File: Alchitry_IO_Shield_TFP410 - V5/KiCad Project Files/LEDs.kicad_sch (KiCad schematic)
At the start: 52 parts, among them Q1 Q_PMOS_SGD, Q2 Q_PMOS_SGD, Q3 Q_PMOS_SGD, Q4 Q_PMOS_SGD, SW1 SWL3, SW10 SW_DIP_x08, SW2 SWL1, SW3 SWL2, SW4 SWL4, SW5 SWR3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

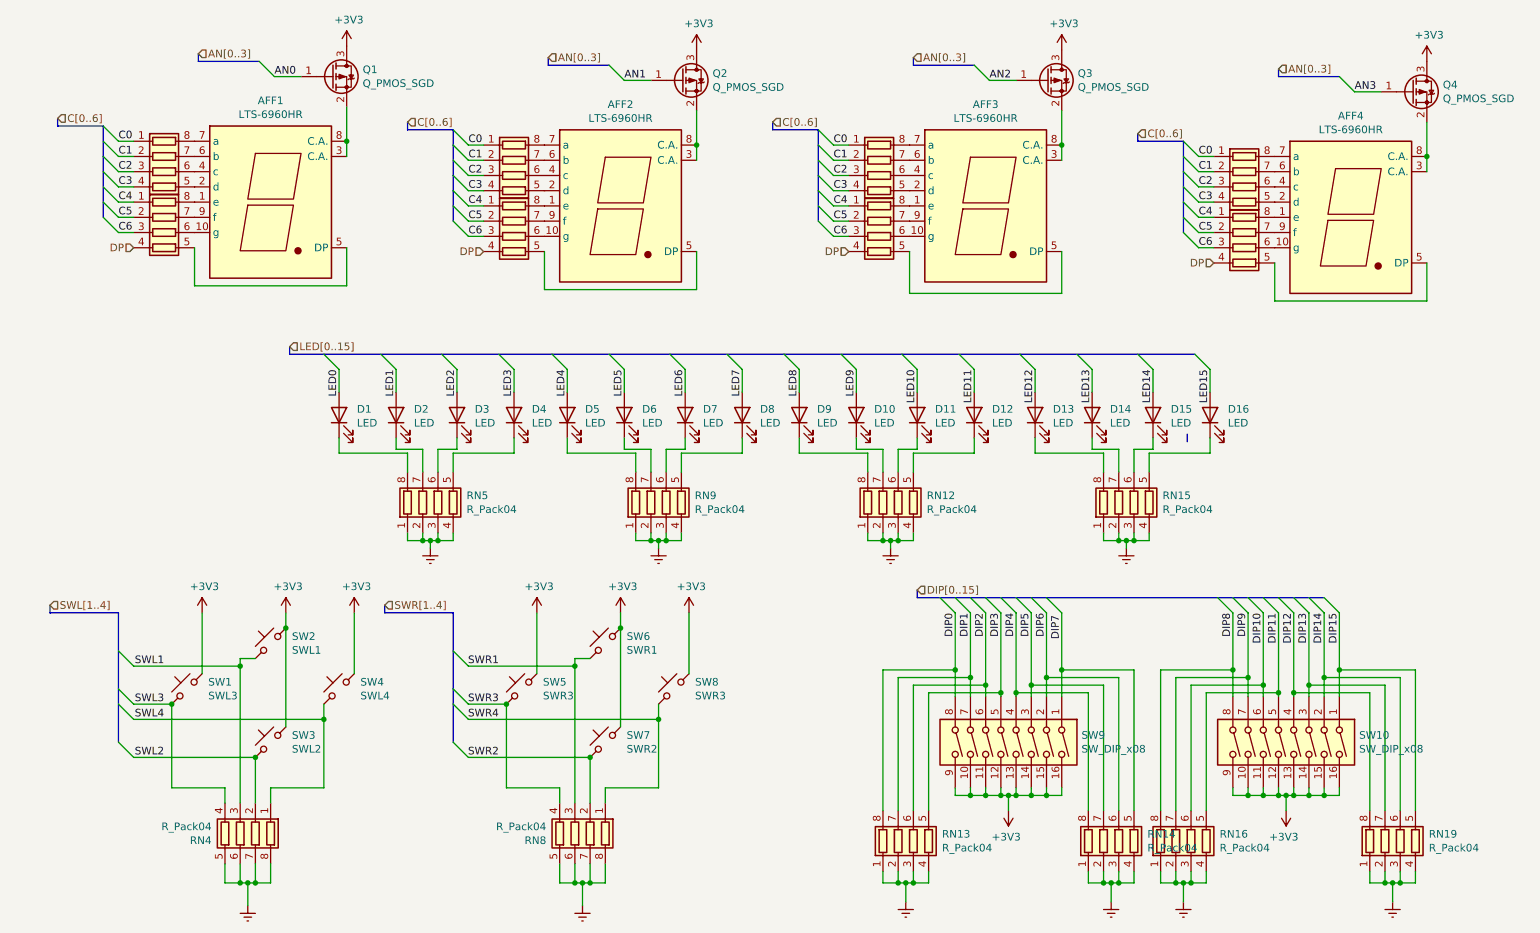
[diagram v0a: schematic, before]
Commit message: grouped footprints by function
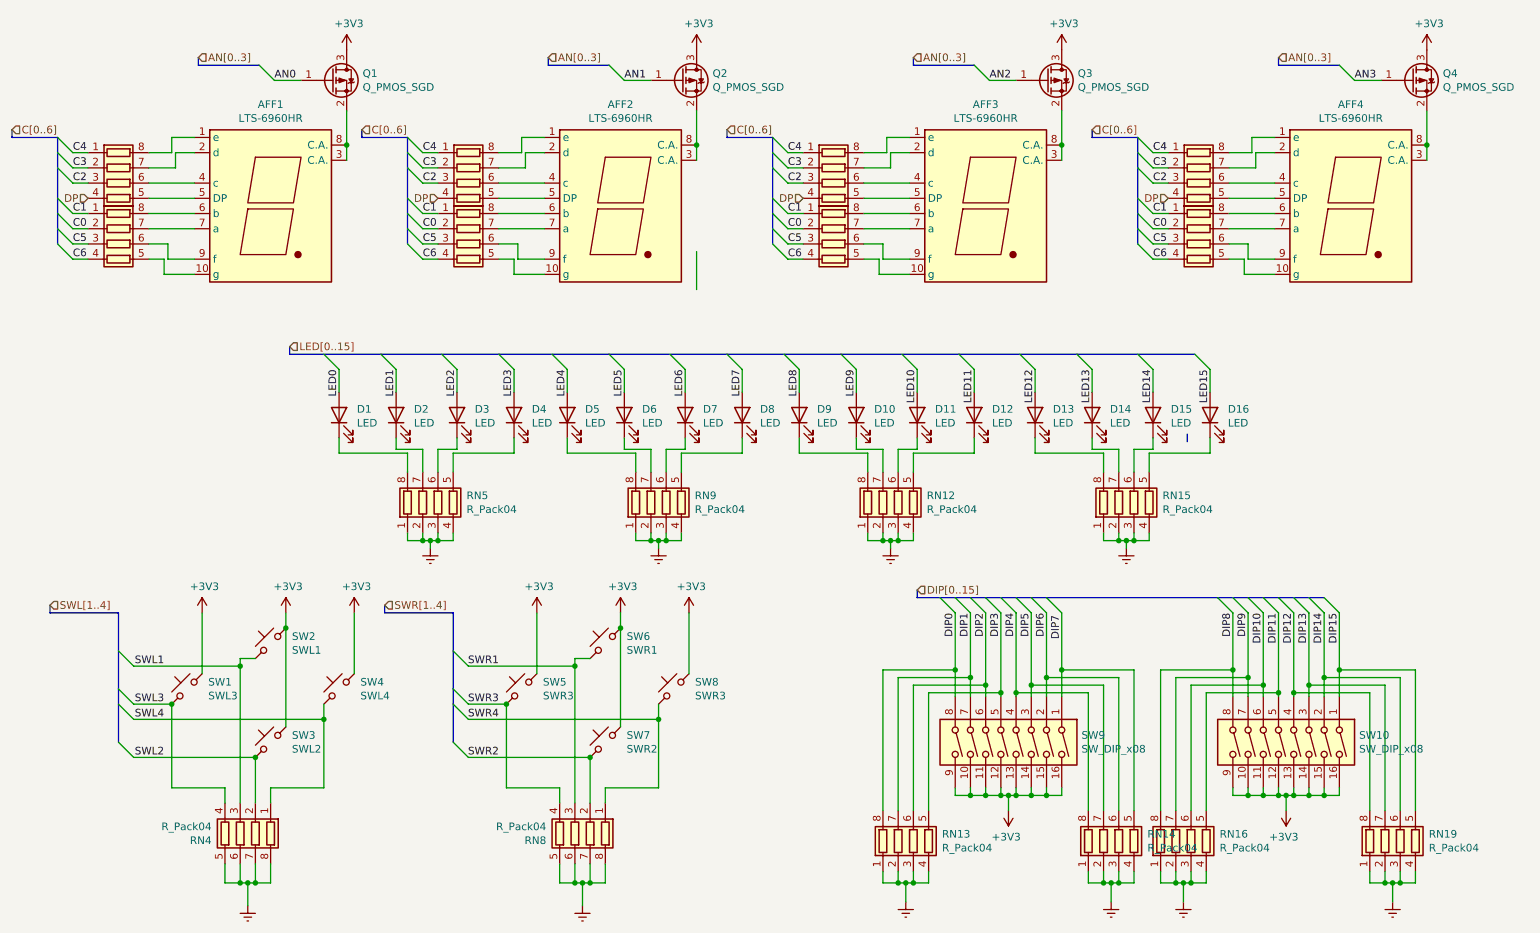
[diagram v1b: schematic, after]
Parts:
- AFF1, AFF2, AFF3, AFF4: footprint Display_7Segment:KCSC02-136 -> Display_7Segment:KCSC02-105; symbol Display_Character:LTS-6960HR -> 7_Segment_LTS6780:LTS-6960HR
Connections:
- net C0: now also RN11.2 (R2.1), RN18.2 (R2.1), RN3.2 (R2.1), RN7.2 (R2.1); no longer RN10.1 (R1.1), RN17.1 (R1.1), RN2.1 (R1.1), RN6.1 (R1.1)
- net C1: now also RN11.1 (R1.1), RN18.1 (R1.1), RN3.1 (R1.1), RN7.1 (R1.1); no longer RN10.2 (R2.1), RN17.2 (R2.1), RN2.2 (R2.1), RN6.2 (R2.1)
- net C3: now also RN10.2 (R2.1), RN17.2 (R2.1), RN2.2 (R2.1), RN6.2 (R2.1); no longer RN10.4 (R4.1), RN17.4 (R4.1), RN2.4 (R4.1), RN6.4 (R4.1)
- net C4: now also RN10.1 (R1.1), RN17.1 (R1.1), RN2.1 (R1.1), RN6.1 (R1.1); no longer RN11.1 (R1.1), RN18.1 (R1.1), RN3.1 (R1.1), RN7.1 (R1.1)
- net C5: now also RN11.3 (R3.1), RN18.3 (R3.1), RN3.3 (R3.1), RN7.3 (R3.1); no longer RN11.2 (R2.1), RN18.2 (R2.1), RN3.2 (R2.1), RN7.2 (R2.1)
- net C6: now also RN11.4 (R4.1), RN18.4 (R4.1), RN3.4 (R4.1), RN7.4 (R4.1); no longer RN11.3 (R3.1), RN18.3 (R3.1), RN3.3 (R3.1), RN7.3 (R3.1)
- net DP: now also RN10.4 (R4.1), RN17.4 (R4.1), RN2.4 (R4.1), RN6.4 (R4.1); no longer RN11.4 (R4.1), RN18.4 (R4.1), RN3.4 (R4.1), RN7.4 (R4.1)
- net at AFF1.1 (e): now also RN2.8 (R1.2); no longer RN3.8 (R1.2)
- net at AFF1.10 (g): now also RN3.5 (R4.2); no longer RN3.6 (R3.2)
- net at AFF1.2 (d): now also RN2.7 (R2.2); no longer RN2.5 (R4.2)
- net at AFF1.5 (DP): now also RN2.5 (R4.2); no longer RN3.5 (R4.2)
- net at AFF1.6 (b): now also RN3.8 (R1.2); no longer RN2.7 (R2.2)
- net at AFF1.7 (a): now also RN3.7 (R2.2); no longer RN2.8 (R1.2)
- net at AFF1.9 (f): now also RN3.6 (R3.2); no longer RN3.7 (R2.2)
- net at AFF2.1 (e): now also RN6.8 (R1.2); no longer RN7.8 (R1.2)
- net at AFF2.10 (g): now also RN7.5 (R4.2); no longer RN7.6 (R3.2)
- net at AFF2.2 (d): now also RN6.7 (R2.2); no longer RN6.5 (R4.2)
- net at AFF2.5 (DP): now also RN6.5 (R4.2); no longer RN7.5 (R4.2)
- net at AFF2.6 (b): now also RN7.8 (R1.2); no longer RN6.7 (R2.2)
- net at AFF2.7 (a): now also RN7.7 (R2.2); no longer RN6.8 (R1.2)
- net at AFF2.9 (f): now also RN7.6 (R3.2); no longer RN7.7 (R2.2)
- net at AFF3.1 (e): now also RN10.8 (R1.2); no longer RN11.8 (R1.2)
- net at AFF3.10 (g): now also RN11.5 (R4.2); no longer RN11.6 (R3.2)
- net at AFF3.2 (d): now also RN10.7 (R2.2); no longer RN10.5 (R4.2)
- net at AFF3.5 (DP): now also RN10.5 (R4.2); no longer RN11.5 (R4.2)
- net at AFF3.6 (b): now also RN11.8 (R1.2); no longer RN10.7 (R2.2)
- net at AFF3.7 (a): now also RN11.7 (R2.2); no longer RN10.8 (R1.2)
- net at AFF3.9 (f): now also RN11.6 (R3.2); no longer RN11.7 (R2.2)
- net at AFF4.1 (e): now also RN17.8 (R1.2); no longer RN18.8 (R1.2)
- net at AFF4.10 (g): now also RN18.5 (R4.2); no longer RN18.6 (R3.2)
- net at AFF4.2 (d): now also RN17.7 (R2.2); no longer RN17.5 (R4.2)
- net at AFF4.5 (DP): now also RN17.5 (R4.2); no longer RN18.5 (R4.2)
- net at AFF4.6 (b): now also RN18.8 (R1.2); no longer RN17.7 (R2.2)
- net at AFF4.7 (a): now also RN18.7 (R2.2); no longer RN17.8 (R1.2)
- net at AFF4.9 (f): now also RN18.6 (R3.2); no longer RN18.7 (R2.2)
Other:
- moved on the sheet: AFF4, Q1, Q4

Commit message: started new shield
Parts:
- removed AFF1, AFF2, AFF3, AFF4: LTS-6960HR, Display_7Segment:KCSC02-105, symbol 7_Segment_LTS6780:LTS-6960HR
- removed RN10, RN11, RN17, RN18, RN2, RN3, RN6, RN7: R_Pack04, Resistor_SMD:R_Array_Convex_4x0603, symbol Device:R_Pack04
- added U3, U4, U5, U6: 0402_7Seg_CA, Custom_LEDs:0402_7Seg_CA_W_Res, symbol Custom_LEDs:0402_7Seg_CA_W_Res
- D1, D10, D11, D12, D13, D14, D15, D16, D2, D3, D4, D5, D6, D7, D8, D9: footprint LED_SMD:LED_0603_1608Metric_Pad1.05x0.95mm_HandSolder -> LED_SMD:LED_0402_1005Metric
- SW1, SW2, SW3, SW4, SW5, SW6, SW7, SW8: footprint Button_Switch_SMD:SW_SPST_TL3342 -> Custom_Buttons:Korean Hroparts Elec K2-1177SR
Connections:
- net C0: now also U3.1 (a), U4.1 (a), U5.1 (a), U6.1 (a)
- net C1: now also U3.2 (b), U4.2 (b), U5.2 (b), U6.2 (b)
- net C2: now also U3.3 (c), U4.3 (c), U5.3 (c), U6.3 (c)
- net C3: now also U3.4 (d), U4.4 (d), U5.4 (d), U6.4 (d)
- net C4: now also U3.5 (e), U4.5 (e), U5.5 (e), U6.5 (e)
- net C5: now also U3.6 (f), U4.6 (f), U5.6 (f), U6.6 (f)
- net C6: now also U3.7 (g), U4.7 (g), U5.7 (g), U6.7 (g)
- net SWL1: now also RN4.1 (R1.1); no longer RN4.3 (R3.1)
- net SWL2: now also RN4.3 (R3.1); no longer RN4.2 (R2.1)
- net SWL3: now also RN4.2 (R2.1); no longer RN4.4 (R4.1)
- net SWL4: now also RN4.4 (R4.1); no longer RN4.1 (R1.1)
- net SWR1: now also RN8.1 (R1.1); no longer RN8.3 (R3.1)
- net SWR2: now also RN8.3 (R3.1); no longer RN8.2 (R2.1)
- net SWR3: now also RN8.2 (R2.1); no longer RN8.4 (R4.1)
- net SWR4: now also RN8.4 (R4.1); no longer RN8.1 (R1.1)
- net at Q1.2 (S): now also U3.8 (C.A.)
- net at Q2.2 (S): now also U4.8 (C.A.)
- net at Q3.2 (S): now also U5.8 (C.A.)
- net at Q4.2 (S): now also U6.8 (C.A.)
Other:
- moved on the sheet: D1, D10, D11, D12, D13, D14, D15, D16, D2, D3, D4, D5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

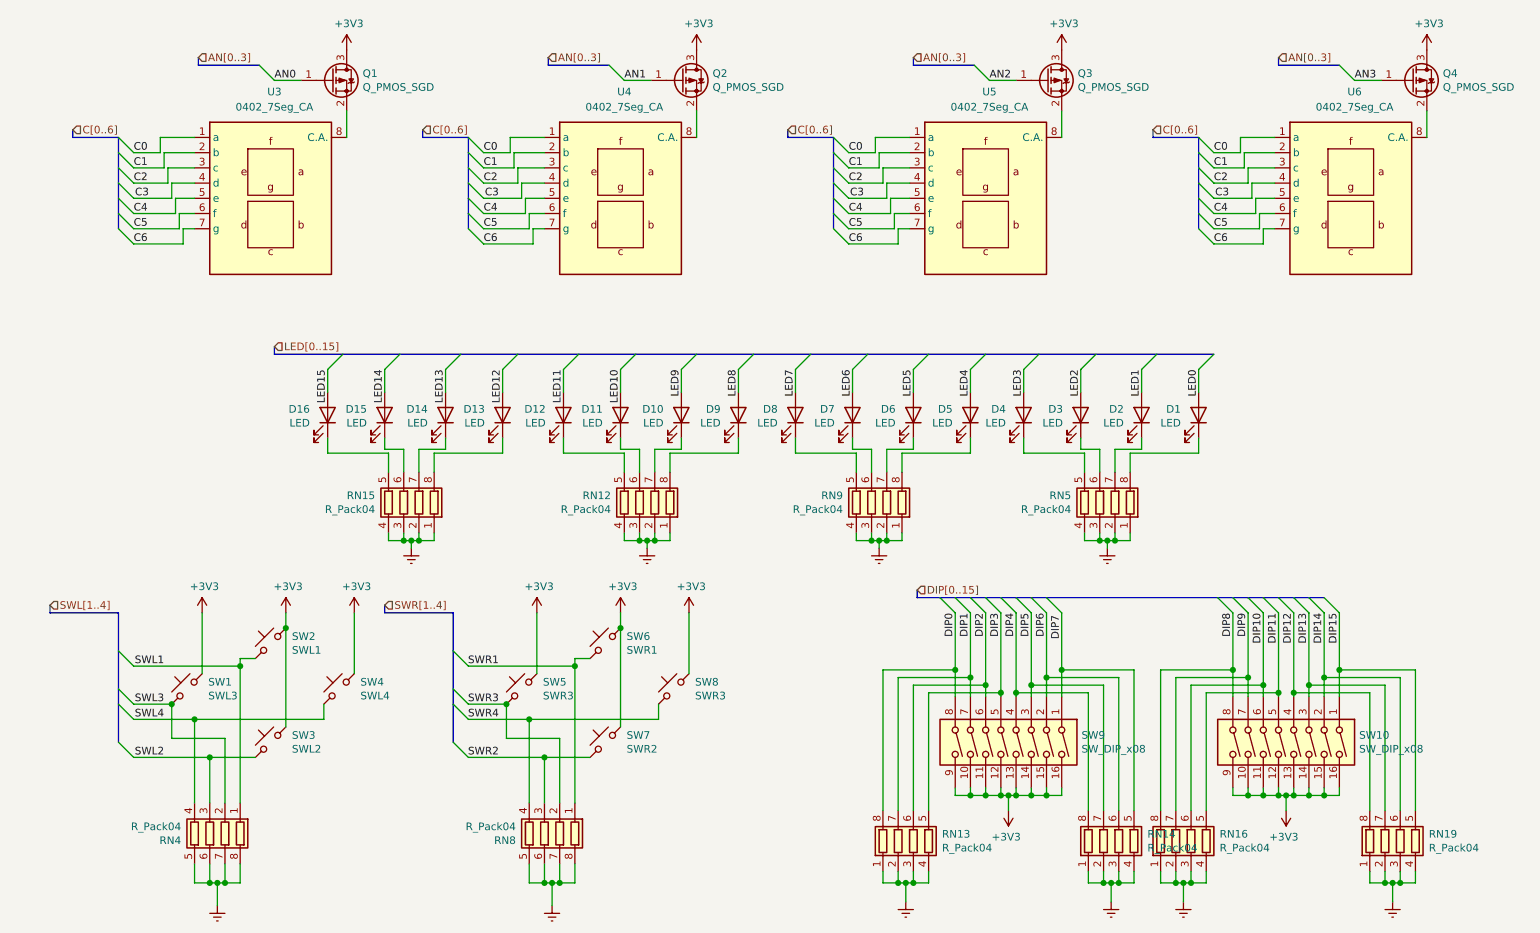
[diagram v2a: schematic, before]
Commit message: replaced 7segs with custom footprints
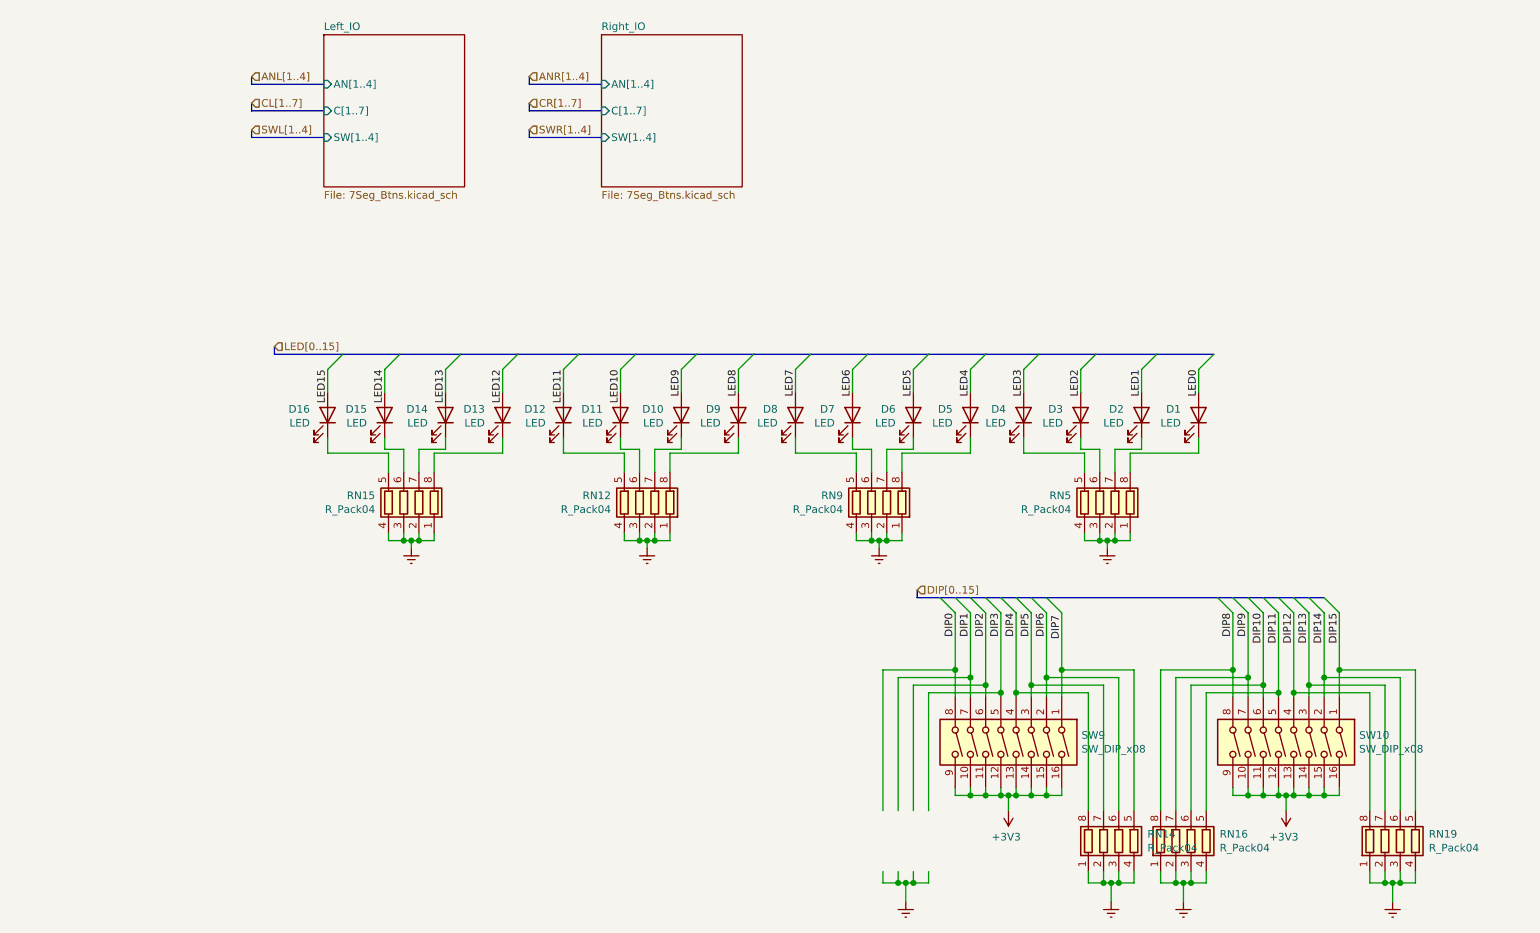
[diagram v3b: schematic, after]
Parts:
- removed Q1, Q2, Q3, Q4: Q_PMOS_SGD, Package_TO_SOT_SMD:SOT-23, symbol Device:Q_PMOS_GSD
- removed RN13, RN4, RN8: R_Pack04, Resistor_SMD:R_Array_Convex_4x0603, symbol Device:R_Pack04
- removed SW1: SWL3, Custom_Buttons:Korean Hroparts Elec K2-1177SR, symbol Switch:SW_Push_45deg
- removed SW2: SWL1, Custom_Buttons:Korean Hroparts Elec K2-1177SR, symbol Switch:SW_Push_45deg
- removed SW3: SWL2, Custom_Buttons:Korean Hroparts Elec K2-1177SR, symbol Switch:SW_Push_45deg
- removed SW4: SWL4, Custom_Buttons:Korean Hroparts Elec K2-1177SR, symbol Switch:SW_Push_45deg
- removed SW5, SW8: SWR3, Custom_Buttons:Korean Hroparts Elec K2-1177SR, symbol Switch:SW_Push_45deg
- removed SW6: SWR1, Custom_Buttons:Korean Hroparts Elec K2-1177SR, symbol Switch:SW_Push_45deg
- removed SW7: SWR2, Custom_Buttons:Korean Hroparts Elec K2-1177SR, symbol Switch:SW_Push_45deg
- removed U3, U4, U5, U6: 0402_7Seg_CA, Custom_LEDs:0402_7Seg_CA_W_Res, symbol Custom_LEDs:0402_7Seg_CA_W_Res
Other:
- added sheet Left_IO (7Seg_Btns.kicad_sch)
- added sheet Right_IO (7Seg_Btns.kicad_sch)

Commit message: laid out switches, btns and leds
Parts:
- added RN4: R_Pack04, Resistor_SMD:R_Array_Convex_4x0603, symbol Device:R_Pack04
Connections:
- net DIP0 is gone; now on net DIP9: SW9.8
- net LED0 is gone; now on net LED1: D1.2 (A)
- net DIP1: now also RN16.5 (R4.2), SW10.8; no longer SW9.7
- net DIP10: now also SW9.7, RN4.6 (R3.2); no longer RN16.6 (R3.2), SW10.6
- net DIP11: now also SW9.6, RN4.7 (R2.2); no longer RN16.5 (R4.2), SW10.5
- net DIP12: now also SW9.5, RN4.8 (R1.2); no longer RN19.8 (R1.2), SW10.4
- net DIP13: now also RN14.5 (R4.2), SW9.4; no longer RN19.7 (R2.2), SW10.3
- net DIP14: now also RN14.6 (R3.2), SW9.3; no longer RN19.6 (R3.2), SW10.2
- net DIP15: now also RN14.7 (R2.2), SW9.2; no longer RN19.5 (R4.2), SW10.1
- net DIP2: now also RN16.6 (R3.2), SW10.7; no longer SW9.6
- net DIP3: now also RN16.7 (R2.2), SW10.6; no longer SW9.5
- net DIP4: now also RN16.8 (R1.2), SW10.5; no longer RN14.8 (R1.2), SW9.4
- net DIP5: now also RN19.5 (R4.2), SW10.4; no longer RN14.7 (R2.2), SW9.3
- net DIP6: now also RN19.6 (R3.2), SW10.3; no longer RN14.6 (R3.2), SW9.2
- net DIP7: now also RN19.7 (R2.2), SW10.2; no longer RN14.5 (R4.2), SW9.1
- net DIP8: now also RN19.8 (R1.2), SW10.1; no longer RN16.8 (R1.2), SW10.8
- net DIP9: now also RN4.5 (R4.2); no longer RN16.7 (R2.2), SW10.7
- net GNDREF: now also RN4.1 (R1.1), RN4.2 (R2.1), RN4.3 (R3.1), RN4.4 (R4.1)
- net LED1: no longer D2.2 (A)
- net LED10: now also D10.2 (A); no longer D11.2 (A)
- net LED11: now also D11.2 (A); no longer D12.2 (A)
- net LED12: now also D12.2 (A); no longer D13.2 (A)
- net LED13: now also D13.2 (A); no longer D14.2 (A)
- net LED14: now also D14.2 (A); no longer D15.2 (A)
- net LED15: now also D15.2 (A); no longer D16.2 (A)
- net LED2: now also D2.2 (A); no longer D3.2 (A)
- net LED3: now also D3.2 (A); no longer D4.2 (A)
- net LED4: now also D4.2 (A); no longer D5.2 (A)
- net LED5: now also D5.2 (A); no longer D6.2 (A)
- net LED6: now also D6.2 (A); no longer D7.2 (A)
- net LED7: now also D7.2 (A); no longer D8.2 (A)
- net LED8: now also D8.2 (A); no longer D9.2 (A)
- net LED9: now also D9.2 (A); no longer D10.2 (A)
- new net DIP16: RN14.8 (R1.2), SW9.1
- new net LED16: D16.2 (A)
